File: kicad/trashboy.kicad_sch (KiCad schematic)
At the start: 8 parts, among them J1 Conn_01x02, X1 TERMBLOCK_1X2

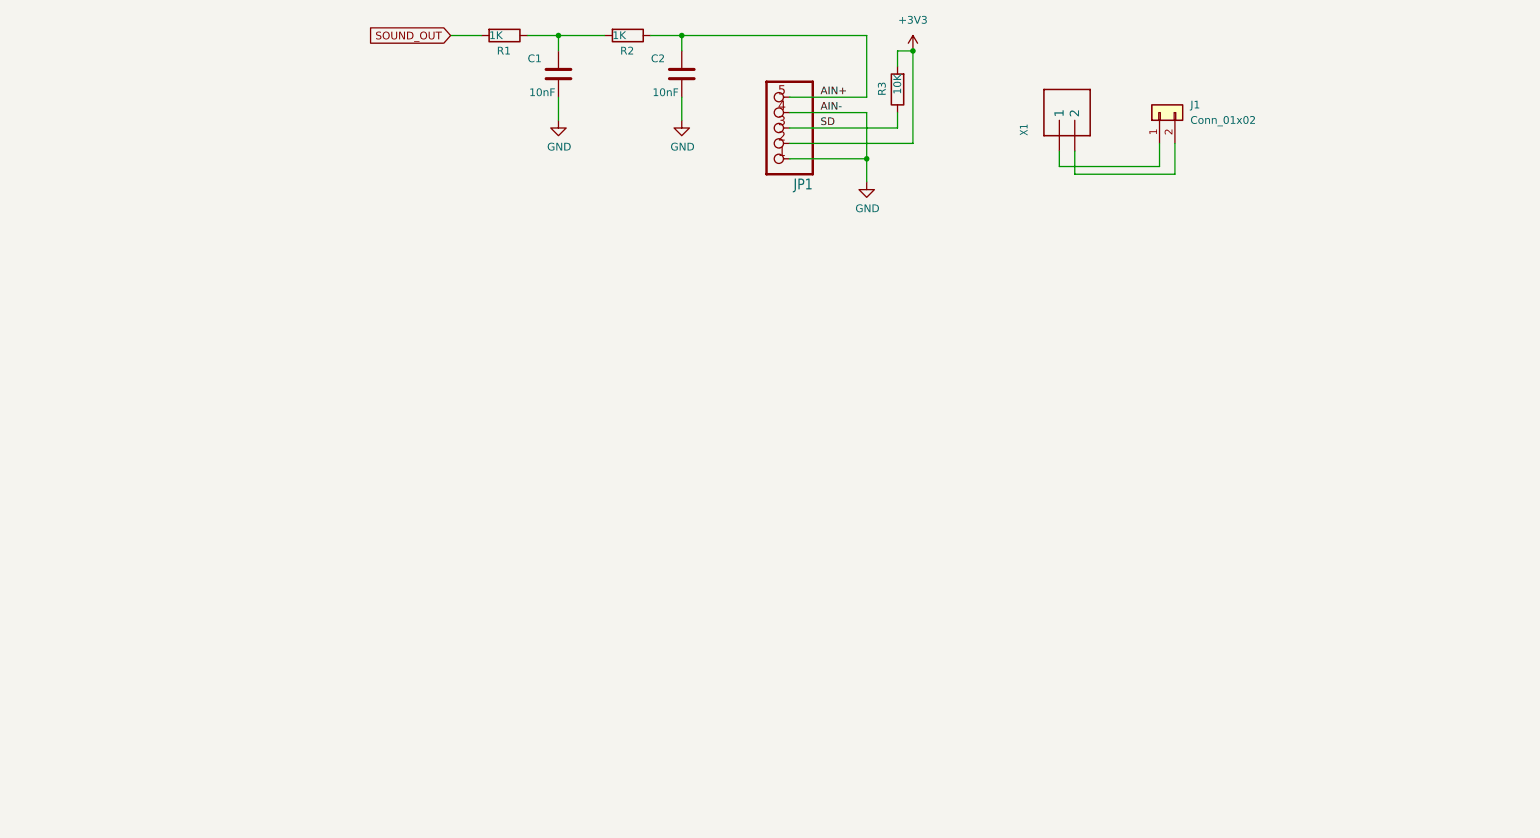
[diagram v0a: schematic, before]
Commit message: Adding all of the component to the schematics.
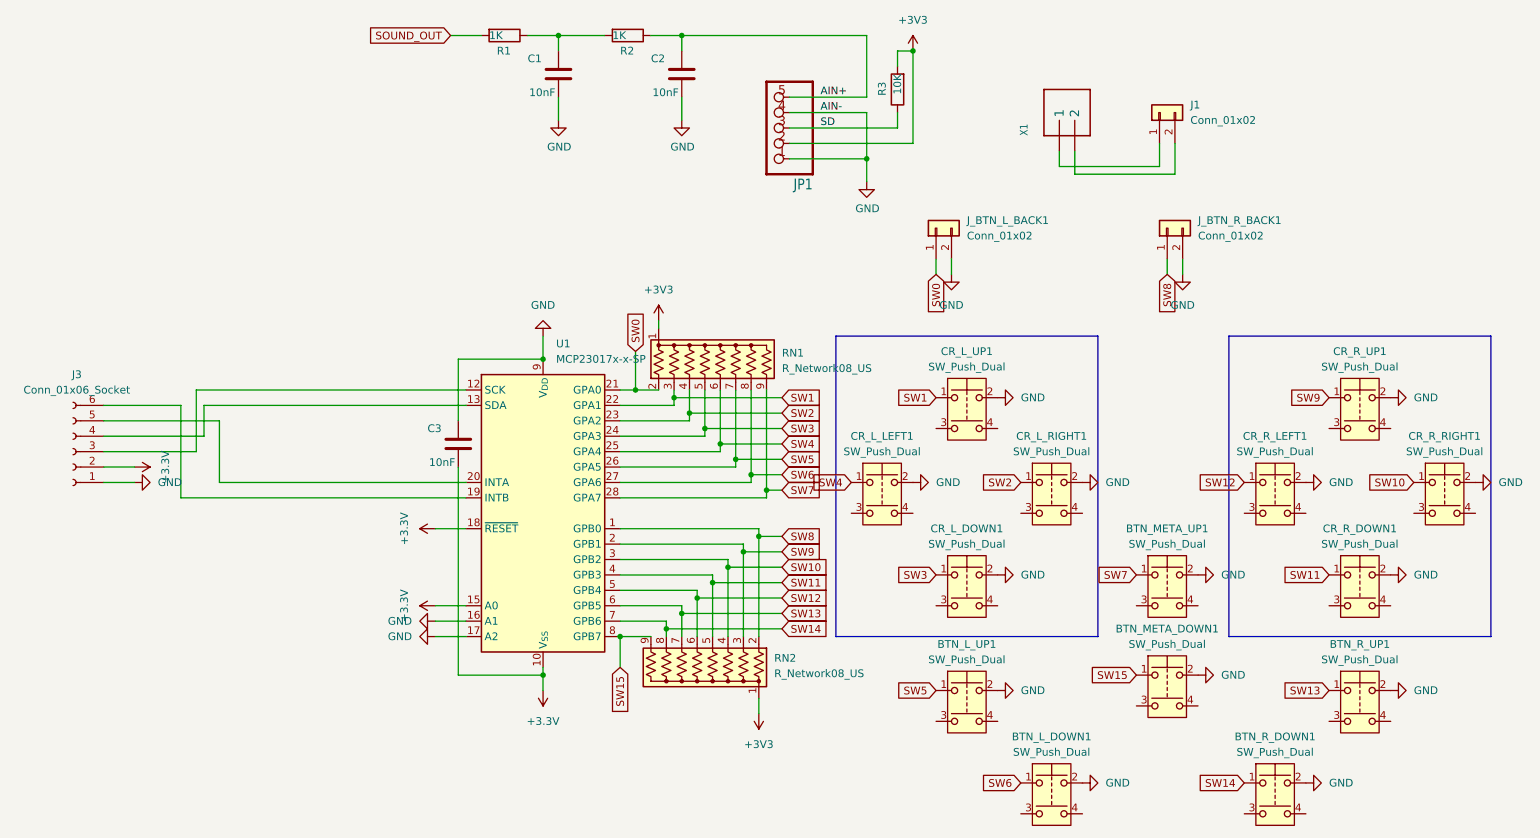
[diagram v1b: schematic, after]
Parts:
- added BTN_L_DOWN1, BTN_L_UP1, BTN_META_DOWN1, BTN_META_UP1, BTN_R_DOWN1, BTN_R_UP1, CR_L_DOWN1, CR_L_LEFT1, CR_L_RIGHT1, CR_L_UP1, CR_R_DOWN1, CR_R_LEFT1, CR_R_RIGHT1, CR_R_UP1: SW_Push_Dual, buttons:SW_Push_Silicone_8x5mm, symbol Switch:SW_Push_Dual
- added C3: 10nF, Capacitor_SMD:C_0805_2012Metric_Pad1.18x1.45mm_HandSolder, symbol Device:C
- added J3: Conn_01x06_Socket, symbol Connector:Conn_01x06_Socket
- added J_BTN_L_BACK1, J_BTN_R_BACK1: Conn_01x02, Connector_PinHeader_2.54mm:PinHeader_1x02_P2.54mm_Vertical, symbol Connector_Generic:Conn_01x02
- added RN1, RN2: R_Network08_US, Resistor_THT:R_Array_SIP9, symbol Device:R_Network08_US
- added U1: MCP23017x-x-SP, Package_DIP:DIP-28_W7.62mm, symbol Interface_Expansion:MCP23017x-x-SP
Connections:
- net +3V3: now also RN1.1 (common), RN2.1 (common)
- net GND: now also BTN_L_DOWN1.2, BTN_L_UP1.2, BTN_META_DOWN1.2, BTN_META_UP1.2, BTN_R_DOWN1.2, BTN_R_UP1.2, C3.1, CR_L_DOWN1.2, CR_L_LEFT1.2, CR_L_RIGHT1.2, CR_L_UP1.2, CR_R_DOWN1.2, CR_R_LEFT1.2, CR_R_RIGHT1.2, CR_R_UP1.2, J3.1 (Pin_1), J_BTN_L_BACK1.2 (Pin_2), J_BTN_R_BACK1.2 (Pin_2), U1.16 (A1), U1.17 (A2), U1.9 (V_{DD})
- new net: J3.3 (Pin_3), U1.12 (SCK)
- new net: J3.4 (Pin_4), U1.13 (SDA)
- new net: J3.5 (Pin_5), U1.20 (INTA)
- new net: J3.6 (Pin_6), U1.19 (INTB)
- new net +3.3V: C3.2, J3.2 (Pin_2), U1.10 (V_{SS}), U1.15 (A0), U1.18 (~{RESET})
- new net SW0: J_BTN_L_BACK1.1 (Pin_1), RN1.2 (R1), U1.21 (GPA0)
- new net SW1: CR_L_UP1.1, RN1.3 (R2), U1.22 (GPA1)
- new net SW10: CR_R_RIGHT1.1, RN2.4 (R3), U1.3 (GPB2)
- new net SW11: CR_R_DOWN1.1, RN2.5 (R4), U1.4 (GPB3)
- new net SW12: CR_R_LEFT1.1, RN2.6 (R5), U1.5 (GPB4)
- new net SW13: BTN_R_UP1.1, RN2.7 (R6), U1.6 (GPB5)
- new net SW14: BTN_R_DOWN1.1, RN2.8 (R7), U1.7 (GPB6)
- new net SW15: BTN_META_DOWN1.1, RN2.9 (R8), U1.8 (GPB7)
- new net SW2: CR_L_RIGHT1.1, RN1.4 (R3), U1.23 (GPA2)
- new net SW3: CR_L_DOWN1.1, RN1.5 (R4), U1.24 (GPA3)
- new net SW4: CR_L_LEFT1.1, RN1.6 (R5), U1.25 (GPA4)
- new net SW5: BTN_L_UP1.1, RN1.7 (R6), U1.26 (GPA5)
- new net SW6: BTN_L_DOWN1.1, RN1.8 (R7), U1.27 (GPA6)
- new net SW7: BTN_META_UP1.1, RN1.9 (R8), U1.28 (GPA7)
- new net SW8: J_BTN_R_BACK1.1 (Pin_1), RN2.2 (R1), U1.1 (GPB0)
- new net SW9: CR_R_UP1.1, RN2.3 (R2), U1.2 (GPB1)

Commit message: First attempt to place all the components, no traces yet.
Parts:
- J3: footprint (none) -> Connector_PinHeader_2.54mm:PinHeader_1x06_P2.54mm_Vertical
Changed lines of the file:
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@@
 			)
 		)
-		(property "Footprint" ""
+		(property "Footprint" "Connector_PinHeader_2.54mm:PinHeader_1x06_P2.54mm_Vertical"
 			(at 21.59 105.41 0)
 			(hide yes)

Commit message: finished the PCB design and exported fabrication files.
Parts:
- removed J3: Conn_01x06_Socket, Connector_PinHeader_2.54mm:PinHeader_1x06_P2.54mm_Vertical, symbol Connector:Conn_01x06_Socket
- added J2: Conn_01x07_Socket, Connector_PinHeader_2.54mm:PinHeader_1x07_P2.54mm_Vertical, symbol Connector:Conn_01x07_Socket
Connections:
- net +3.3V: now also J2.2 (Pin_2)
- net GND: now also J2.1 (Pin_1)
- net SOUND_OUT: now also J2.7 (Pin_7)
- net at U1.12 (SCK): now also J2.3 (Pin_3)
- net at U1.13 (SDA): now also J2.4 (Pin_4)
- net at U1.20 (INTA): now also J2.5 (Pin_5)
- net at U1.19 (INTB): now also J2.6 (Pin_6)
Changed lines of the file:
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@@
 		)
 	)
+	(global_label "SOUND_OUT"
+		(shape input)
+		(at 26.67 95.25 0)
+		(fields_autoplaced yes)
+		(effects
+			(font
+				(size 1.27 1.27)
+			)
+			(justify left)
+		)
+		(property "Intersheetrefs" "${INTERSHEET_REFS}"
+			(at 40.7224 95.25 0)
+			(hide yes)
+			(show_name no)
+			(do_not_autoplace no)
+			(effects
+				(font
+					(size 1.27 1.27)
+				)
+				(justify left)
+			)
+		)
+	)
 	(global_label "SW12"
 		(shape input)
@@
 	)
 	(symbol
-		(lib_id "Connector:Conn_01x06_Socket")
-		(at 21.59 105.41 180)
-		(unit 1)
-		(body_style 1)
-		(exclude_from_sim no)
-		(in_bom yes)
-		(on_board yes)
-		(in_pos_files yes)
-		(dnp no)
-		(fields_autoplaced yes)
-		(property "Reference" "J3"
-			(at 22.225 92.71 0)
-			(show_name no)
-			(do_not_autoplace no)
-			(effects
-				(font
-					(size 1.27 1.27)
-				)
-			)
-		)
-		(property "Value" "Conn_01x06_Socket"
-			(at 22.225 95.25 0)
-			(show_name no)
-			(do_not_autoplace no)
-			(effects
-				(font
-					(size 1.27 1.27)
-				)
-			)
-		)
-		(property "Footprint" "Connector_PinHeader_2.54mm:PinHeader_1x06_P2.54mm_Vertical"
-			(at 21.59 105.41 0)
-			(hide yes)
-			(show_name no)
-			(do_not_autoplace no)
-			(effects
-				(font
-					(size 1.27 1.27)
-				)
-			)
-		)
-		(property "Datasheet" ""
-			(at 21.59 105.41 0)
-			(hide yes)
-			(show_name no)
-			(do_not_autoplace no)
-			(effects
-				(font
-					(size 1.27 1.27)
-				)
-			)
-		)
-		(property "Description" "Generic connector, single row, 01x06, script generated"
-			(at 21.59 105.41 0)
-			(hide yes)
-			(show_name no)
-			(do_not_autoplace no)
-			(effects
-				(font
-					(size 1.27 1.27)
-				)
-			)
-		)
-		(pin "1"
-		)
-		(pin "4"
-		)
-		(pin "5"
-		)
-		(pin "6"
-		)
-		(pin "3"
-		)
-		(pin "2"
-		)
-		(instances
-			(project "trashboy"
-				(path "/1f0bf014-b3ca-458c-bbf9-be25b9651a91"
-					(reference "J3")
-					(unit 1)
-				)
-			)
-		)
-	)
-	(symbol
 		(lib_name "GND_1")
 		(lib_id "power:GND")
@@
 					(unit 1)
 				)
+			)
+		)
+	)
+	(symbol
+		(lib_id "Connector:Conn_01x07_Socket")
+		(at 21.59 102.87 180)
+		(unit 1)
+		(body_style 1)
+		(exclude_from_sim no)
+		(in_bom yes)
+		(on_board yes)
+		(in_pos_files yes)
+		(dnp no)
+		(fields_autoplaced yes)
+		(property "Reference" "J2"
+			(at 22.225 90.17 0)
+			(show_name no)
+			(do_not_autoplace no)
+			(effects
+				(font
+					(size 1.27 1.27)
+				)
+			)
+		)
+		(property "Value" "Conn_01x07_Socket"
+			(at 22.225 92.71 0)
+			(show_name no)
+			(do_not_autoplace no)
+			(effects
+				(font
+					(size 1.27 1.27)
+				)
+			)
+		)
+		(property "Footprint" "Connector_PinHeader_2.54mm:PinHeader_1x07_P2.54mm_Vertical"
+			(at 21.59 102.87 0)
+			(hide yes)
+			(show_name no)
+			(do_not_autoplace no)
+			(effects
+				(font
+					(size 1.27 1.27)
+				)
+			)
+		)
+		(property "Datasheet" ""
+			(at 21.59 102.87 0)
+			(hide yes)
+			(show_name no)
+			(do_not_autoplace no)
+			(effects
+				(font
+					(size 1.27 1.27)
+				)
+			)
+		)
+		(property "Description" "Generic connector, single row, 01x07, script generated"
+			(at 21.59 102.87 0)
+			(hide yes)
+			(show_name no)
+			(do_not_autoplace no)
+			(effects
+				(font
+					(size 1.27 1.27)
+				)
+			)
+		)
+		(pin "4"
+		)
+		(pin "2"
+		)
+		(pin "3"
+		)
+		(pin "1"
+		)
+		(pin "5"
+		)
+		(pin "6"
+		)
+		(pin "7"
+		)
+		(instances
+			(project "trashboy"
+				(path "/1f0bf014-b3ca-458c-bbf9-be25b9651a91"
+					(reference "J2")
+					(unit 1)
+				)
